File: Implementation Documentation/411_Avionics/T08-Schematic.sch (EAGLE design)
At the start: 68 parts, among them IC1 BQ24022, J1 USB-MICROB, J3 JST-PH-2-SMT-RA, U1 LP5907, U2 M25P10-AVMN6TP_TR, U3 LSM9DS0, U5 LTC1998, U6 ATMEGA32U4-AU, X1 8MHz

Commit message: Added pdf for board layout
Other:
- note removed: "- Add Value to VCC **DONE - Change Team Name **DONE - Small bypass caps on power suppliesVCC, AVCC, etc (close to pins) **DONE - Maybe look into hooking up interrupt lines ***DONE - Bypass cap on flash memory **DONE - Add test points ***Ask Andrew: Pads or 0ohm resistors?**Done - Check VBUS**DONE - 11-05-2016"
- note removed: "22 ohm resistors on the D-/D+ lines *** DONE"
- note removed: "A"
- note removed: "Add 6-pin pin header (unless there's a bootloader solution)"
- note removed: "Add LEDs to Stat1/Stat2"
- note removed: "Add user power switch - DONE Add comparator for enable line - DONE Add second LDO for sensor - CANCELED"
- note removed: "NEEDS RGB LED ON GPIO BECAUSE OF REASONS **DONE"
- note removed: "UCAP/UGND - why would they be different"
- note removed: "Understand Data Ready and Data Enable pins"
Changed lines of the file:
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@@
 <sheet>
 <plain>
-<text x="419.1" y="7.366" size="2.54" layer="97">A</text>
 <text x="360.68" y="10.16" size="2.54" layer="97">00000001</text>
 <text x="330.2" y="25.4" size="2.54" layer="97">Model Rocket Avionics, Team 8
@@
 <text x="261.62" y="195.58" size="1.778" layer="97">Sensors</text>
 <text x="261.62" y="236.22" size="1.778" layer="97">Flash Memory</text>
-<text x="403.86" y="45.72" size="2.54" layer="97" rot="R180">All capacitors 16 V rating, ceramic
+<text x="411.48" y="45.72" size="2.54" layer="97" rot="R180">All capacitors 16 V rating, ceramic
 All resistors 1%, high values 1/10W, low values 1/2 W</text>
 <text x="91.44" y="210.82" size="1.778" layer="97" rot="R90">Battery Connector</text>
@@
 <wire x1="96.52" y1="91.44" x2="96.52" y2="198.12" width="0.1524" layer="97"/>
 <wire x1="96.52" y1="198.12" x2="259.08" y2="198.12" width="0.1524" layer="97"/>
-<text x="27.94" y="33.02" size="1.778" layer="97">- Add Value to VCC   **DONE
-- Change Team Name    **DONE
-- Small bypass caps on power suppliesVCC, AVCC, etc (close to pins)  **DONE
-- Maybe look into hooking up interrupt lines ***DONE
-- Bypass cap on flash memory  **DONE
-- Add test points ***Ask Andrew: Pads or 0ohm resistors?**Done
-- Check VBUS**DONE
-- 11-05-2016</text>
-<text x="35.56" y="66.04" size="1.778" layer="97">Add user power switch - DONE
-Add comparator for enable line - DONE
-Add second LDO for sensor - CANCELED</text>
-<text x="27.94" y="27.94" size="1.778" layer="97">NEEDS RGB LED ON GPIO BECAUSE OF REASONS **DONE</text>
 <text x="134.62" y="259.08" size="1.778" layer="97">Low-dropout 3.3V LDO</text>
 <text x="137.668" y="206.756" size="1.778" layer="97">Voltage comparator</text>
@@
 Gyroscope</text>
 <text x="208.28" y="162.56" size="1.778" layer="97">RGB LED</text>
-<text x="38.1" y="134.62" size="1.778" layer="97">Understand Data Ready and Data Enable pins</text>
-<text x="38.1" y="142.24" size="1.778" layer="97">UCAP/UGND - why would they be different</text>
-<text x="38.1" y="137.16" size="1.778" layer="97">22 ohm resistors on the D-/D+ lines *** DONE</text>
-<text x="38.1" y="144.78" size="1.778" layer="97">Add LEDs to Stat1/Stat2</text>
-<text x="38.1" y="139.7" size="1.778" layer="97">Add 6-pin pin header (unless there's a bootloader solution)</text>
 <text x="302.26" y="231.902" size="1.778" layer="97">U2</text>
 <text x="138.938" y="255.778" size="1.778" layer="97">U1</text>

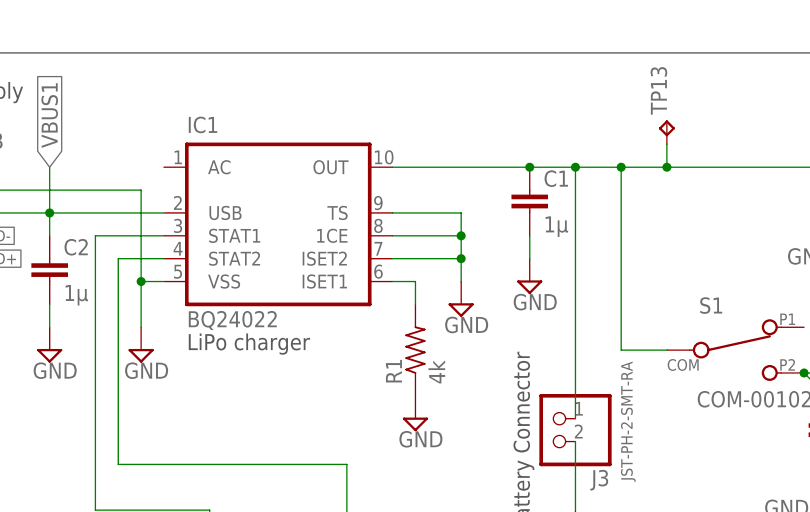
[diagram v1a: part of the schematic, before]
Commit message: Rerouted /PG pin on BQ24022. Corrected symbol and added to eagle library.
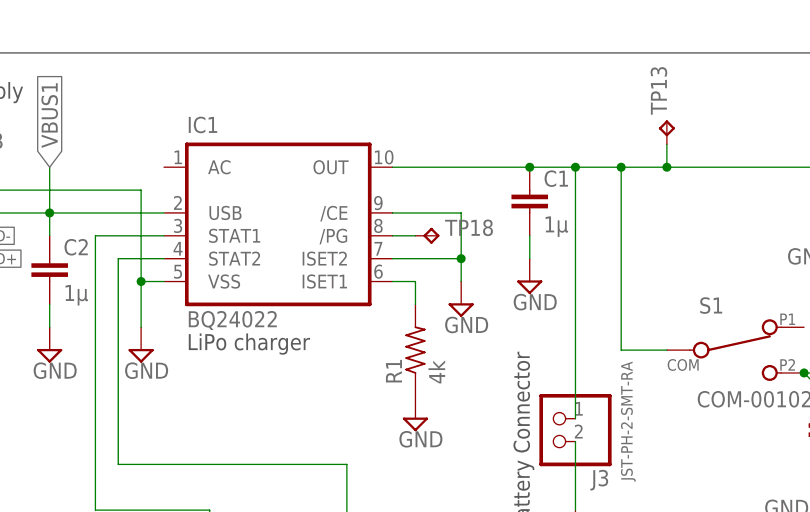
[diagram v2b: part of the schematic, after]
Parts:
- added TP18: TPTP08R, testpad:TPTP08R
- IC1: device texas:BQ24022 -> tinyav-lib:BQ24022
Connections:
- new net N$68: IC1G$1./PG, TP18.TP
- net GND: now also IC1G$1./CE; no longer IC1G$1.1CE, IC1G$1.TS
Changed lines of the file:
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@@
 </classes>
 <parts>
-<part name="IC1" library="texas" deviceset="BQ24022" device=""/>
+<part name="IC1" library="tinyav-lib" deviceset="BQ24022" device=""/>
 <part name="C1" library="rcl" deviceset="C-EU" device="C0603" value="1µ"/>
 <part name="C2" library="rcl" deviceset="C-EU" device="C0805" value="1µ"/>
@@
 <part name="TP16" library="testpad" deviceset="TP" device="TP08R"/>
 <part name="TP17" library="testpad" deviceset="TP" device="TP08R"/>
+<part name="TP18" library="testpad" deviceset="TP" device="TP08R"/>
 </parts>
 <sheets>
@@
 <attribute name="TP_SIGNAL_NAME" x="331.47" y="156.21" size="1.778" layer="97" rot="R270"/>
 </instance>
+<instance part="TP18" gate="G$1" x="81.28" y="243.84" smashed="yes" rot="R270">
+<attribute name="NAME" x="82.042" y="243.84" size="1.778" layer="95"/>
+<attribute name="TP_SIGNAL_NAME" x="80.01" y="242.57" size="1.778" layer="97" rot="R270"/>
+</instance>
 </instances>
 <busses>
@@
 <segment>
 <pinref part="SUPPLY1" gate="GND" pin="GND"/>
-<pinref part="IC1" gate="G$1" pin="1CE"/>
-<wire x1="76.2" y1="243.84" x2="83.82" y2="243.84" width="0.1524" layer="91"/>
-<wire x1="83.82" y1="243.84" x2="83.82" y2="241.3" width="0.1524" layer="91"/>
-<pinref part="IC1" gate="G$1" pin="TS"/>
+<pinref part="IC1" gate="G$1" pin="/CE"/>
 <wire x1="83.82" y1="241.3" x2="83.82" y2="238.76" width="0.1524" layer="91"/>
 <wire x1="76.2" y1="246.38" x2="83.82" y2="246.38" width="0.1524" layer="91"/>
-<wire x1="83.82" y1="246.38" x2="83.82" y2="243.84" width="0.1524" layer="91"/>
-<junction x="83.82" y="243.84"/>
+<wire x1="83.82" y1="246.38" x2="83.82" y2="241.3" width="0.1524" layer="91"/>
 <pinref part="IC1" gate="G$1" pin="ISET2"/>
 <wire x1="76.2" y1="241.3" x2="83.82" y2="241.3" width="0.1524" layer="91"/>
@@
 </segment>
 </net>
+<net name="N$68" class="0">
+<segment>
+<pinref part="IC1" gate="G$1" pin="/PG"/>
+<pinref part="TP18" gate="G$1" pin="TP"/>
+<wire x1="76.2" y1="243.84" x2="78.74" y2="243.84" width="0.1524" layer="91"/>
+</segment>
+</net>
